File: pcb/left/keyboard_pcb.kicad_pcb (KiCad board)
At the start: 2 copper layers, 138.8 x 89.9 mm, 105 parts, among them J3 Alt. Battery, J4 Conn_01x01_Socket, K00 KEYSW, K01 KEYSW, K02 KEYSW, K03 KEYSW, K04 KEYSW, K05 KEYSW, K10 KEYSW, K11 KEYSW, K12 KEYSW, K13 KEYSW, K14 KEYSW, K15 KEYSW, K20 KEYSW, K21 KEYSW, K22 KEYSW, K23 KEYSW, K24 KEYSW, K25 KEYSW, K33 KEYSW, K34 KEYSW, K35 KEYSW, U1 Flippable RP2040 ProMicro/nic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

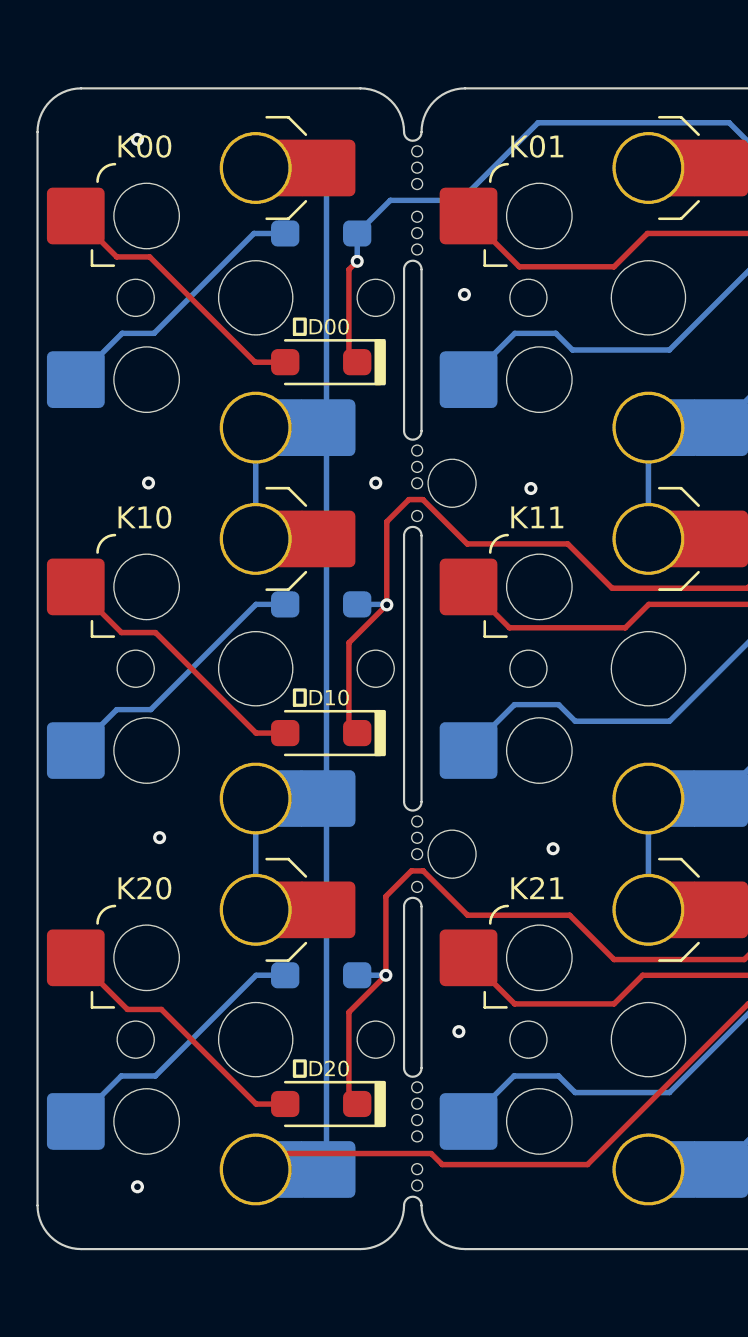
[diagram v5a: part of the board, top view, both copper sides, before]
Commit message: Remove mouse bites
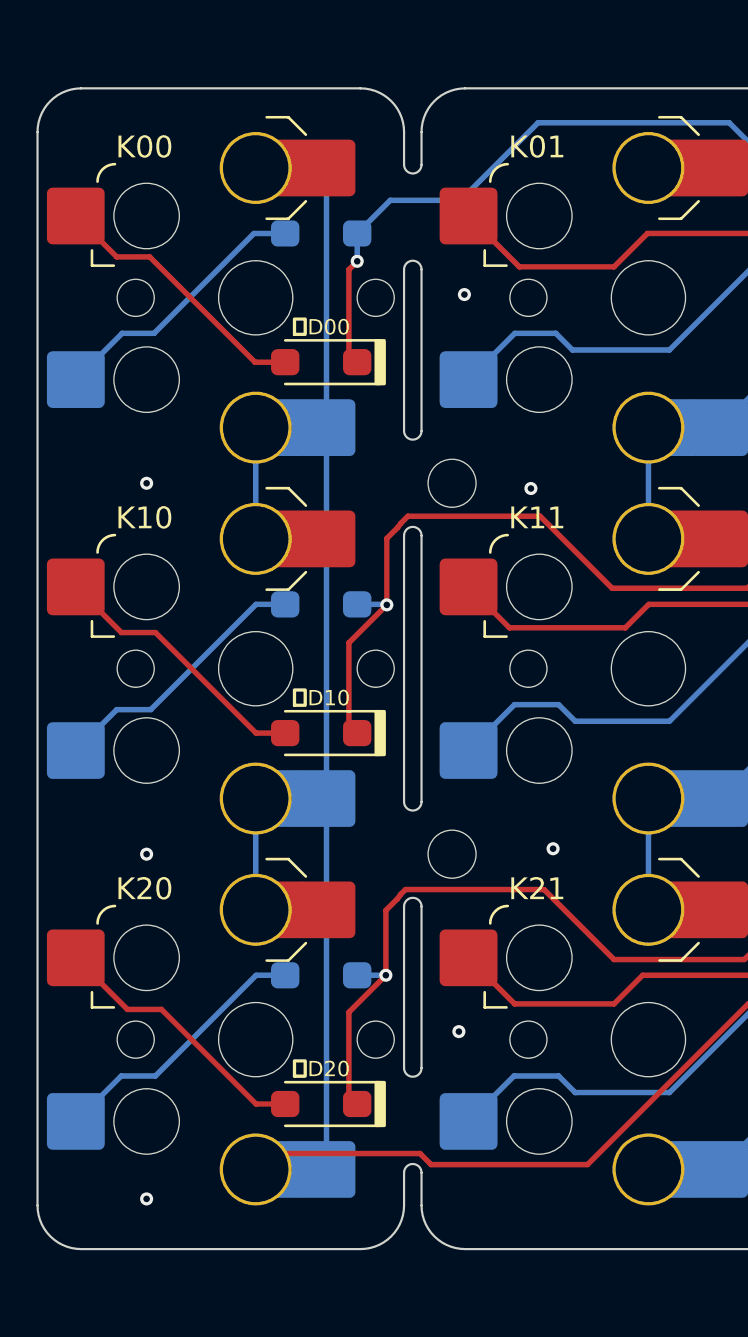
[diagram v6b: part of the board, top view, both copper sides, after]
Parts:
- removed MB1, MB2: MountingHole, beekeeb_lib:mousebites_2
- removed MB3, MB4: MountingHole, beekeeb_lib:mousebites_3
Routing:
- net row1: track 150.5 -> 149.5 mm
- net row2: track 150.1 -> 149.1 mm
- net GND: vias 25 -> 23
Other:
- outline, holes or cut-outs redrawn
